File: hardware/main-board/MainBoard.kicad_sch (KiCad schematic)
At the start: 0 parts

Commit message: feat: top level schem
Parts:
- added CH446Q3: ~, symbol SeniorDesign:CH446Q_Crossbar_Switch
- added R1, R10, R11, R12, R13, R14, R15, R16, R17, R2, R20, R21, R22, R23, R3, R4, R5, R6, R7, R8, R9: R_US, symbol Device:R_US
- added SW1, SW10, SW11, SW12, SW13, SW17, SW18, SW19, SW2, SW3, SW4, SW5, SW6, SW7, SW8, SW9: SW_SPST, symbol Switch:SW_SPST
- added U0, U1, U2, U3, U4: TL071, symbol Amplifier_Operational:TL071
- added U5: STM32F091RCTx, Package_QFP:LQFP-64_10x10mm_P0.5mm, symbol MCU_ST_STM32F0:STM32F091RCTx
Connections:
- net STD/Input: now also CH446Q3.33 (Y0)
- net STD1/Input: now also CH446Q3.35 (Y1)
- new net: R13.2, U0.2 (-)
- new net: R21.2, R22.1, R23.1, U0.3 (+)
- new net: R12.1, SW10.2 (B)
- new net: R3.2, SW3.2 (B)
- new net: R1.2, R2.1, R3.1, U1.3 (+)
- new net: R2.2, SW2.2 (B)
- new net: R21.1, SW17.2 (B)
- new net: R4.2, U1.2 (-)
- new net: R5.1, SW4.2 (B)
- new net: R12.2, R14.1, R15.1, R17.1, U4.3 (+)
- new net: R10.1, R11.1, R9.2, U3.3 (+)
- new net: R11.2, SW9.2 (B)
- new net: R9.1, SW7.2 (B)
- new net: R16.2, U3.2 (-)
- new net: R14.2, SW11.2 (B)
- new net: R20.2, U4.2 (-)
- new net: R22.2, SW18.2 (B)
- new net: R10.2, SW8.2 (B)
- new net: R17.2, SW13.2 (B)
- new net: R15.2, SW12.2 (B)
- new net: R1.1, SW1.2 (B)
- new net: R8.2, U2.2 (-)
- new net: R5.2, R6.1, R7.1, U2.3 (+)
- new net: R6.2, SW5.2 (B)
- new net: U5.18 (VSS), U5.31 (VSS), U5.47 (VSS), U5.63 (VSS)
- new net: R7.2, SW6.2 (B)
- new net: R23.2, SW19.2 (B)
- new net +5V: U0.7 (V+), U1.7 (V+), U2.7 (V+), U3.7 (V+), U4.7 (V+)
- new net -5V: U0.4 (V-), U1.4 (V-), U2.4 (V-), U3.4 (V-), U4.4 (V-)
- new net GND: R13.1, R16.1, R20.1, R4.1, R8.1
- new net STD2/Input: CH446Q3.17 (Y4)
- new net STD3/Input: CH446Q3.39 (Y3)
- new net cell_0_out: SW1.1 (A), SW10.1 (A), SW17.1 (A), SW4.1 (A)
- new net cell_1_out: SW11.1 (A), SW18.1 (A), SW2.1 (A), SW7.1 (A)
- new net cell_2_out: SW12.1 (A), SW19.1 (A), SW5.1 (A), SW8.1 (A)
- new net cell_3_out: SW13.1 (A), SW3.1 (A), SW6.1 (A), SW9.1 (A)
- new net in_0: CH446Q3.31 (X0)
- new net in_1: CH446Q3.30 (X1)
- new net in_2: CH446Q3.29 (X2)
- new net in_3: CH446Q3.28 (X3)
- new net out: CH446Q3.37 (Y2)
- new net sum_012: CH446Q3.26 (X5), U0.6
- new net sum_013: CH446Q3.4 (X7), U1.6
- new net sum_023: CH446Q3.6 (X9), U2.6
- new net sum_123: CH446Q3.8 (X11), U3.6
- new net sum_1234: CH446Q3.24 (X13), U4.6
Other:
- added sheet STD2 (standard_cell.kicad_sch)
- added sheet STD3 (standard_cell.kicad_sch)
- note added: "Summing Amps"

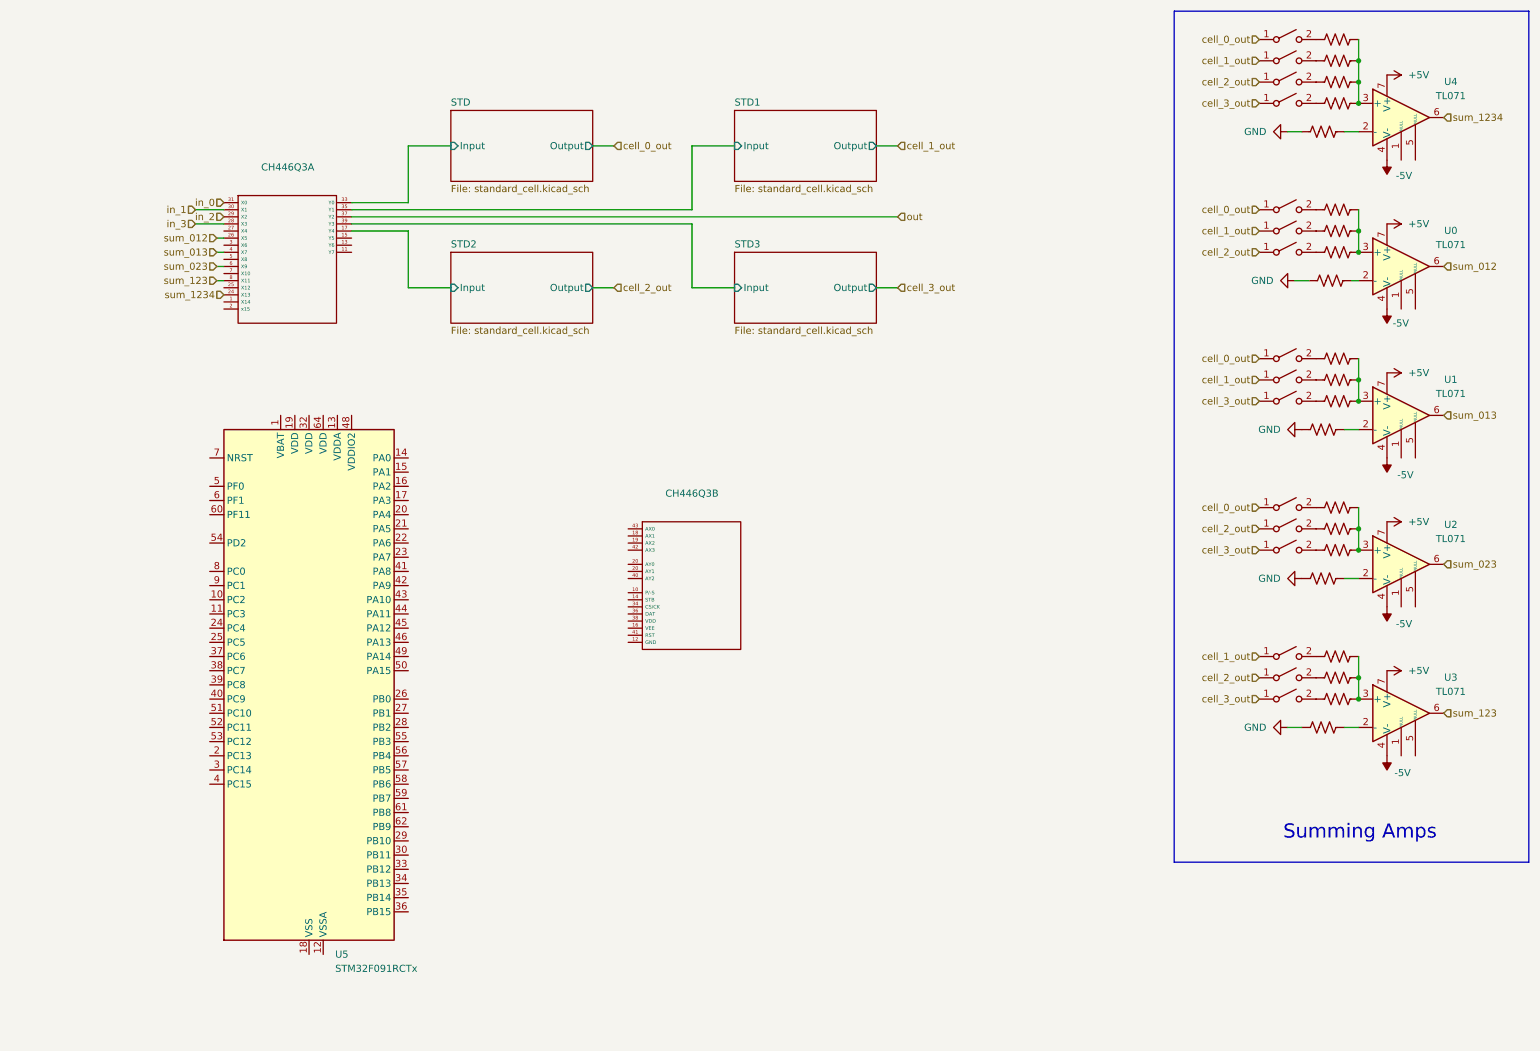
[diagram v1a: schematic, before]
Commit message: fix: top level sectioning
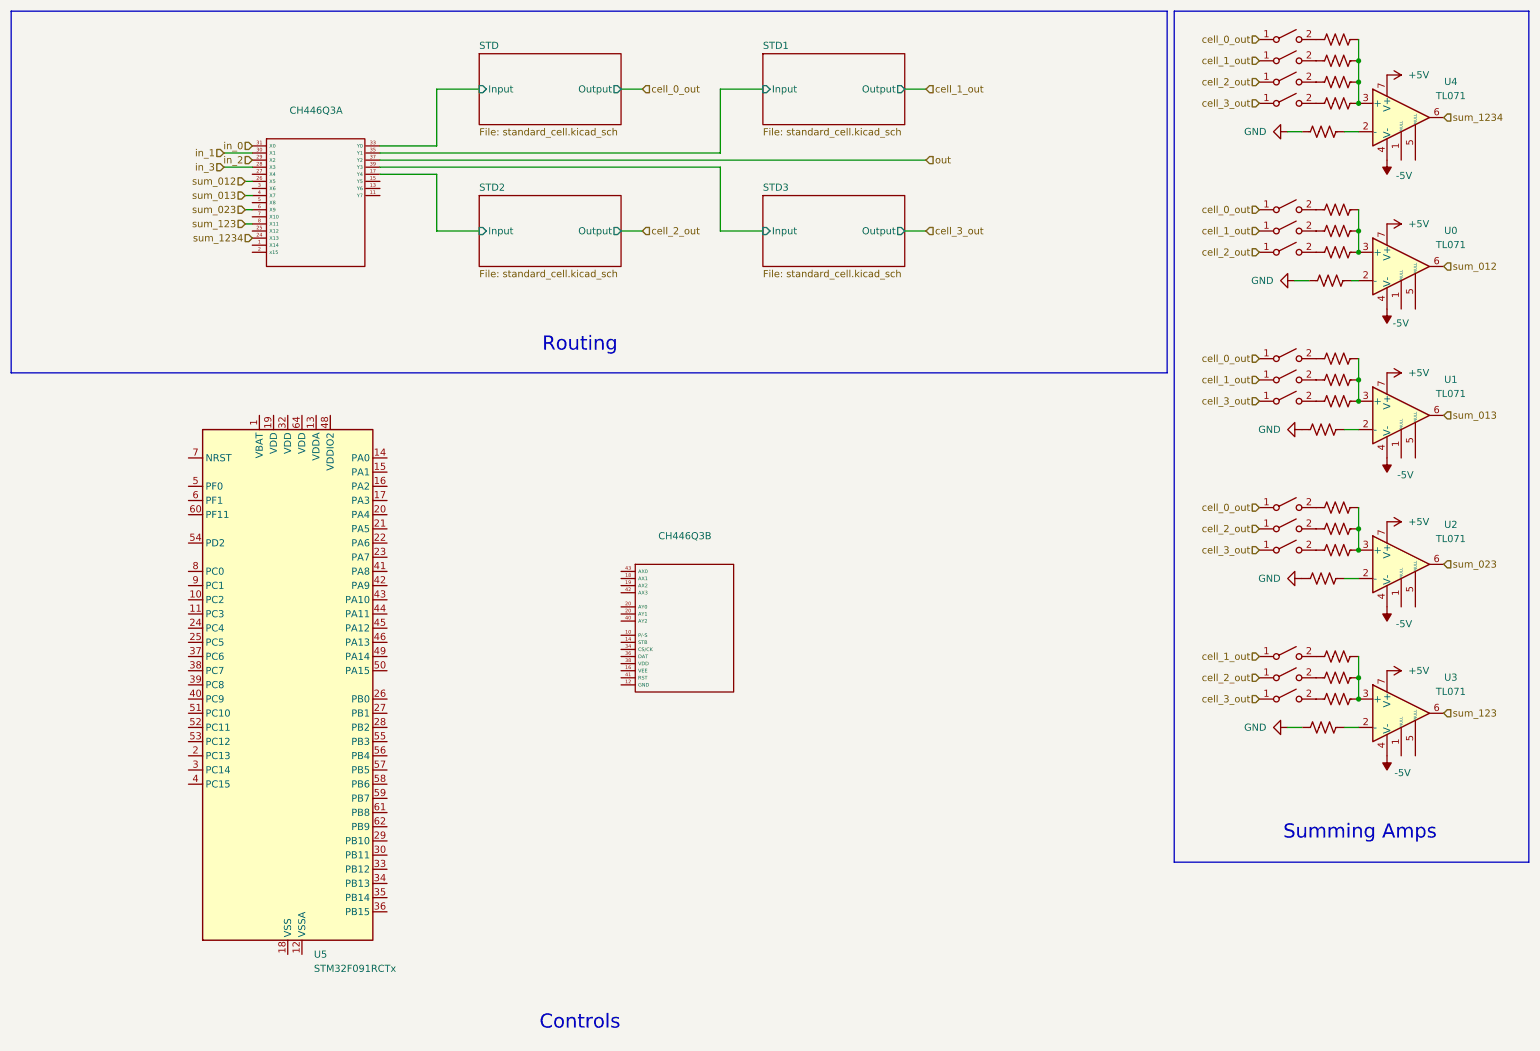
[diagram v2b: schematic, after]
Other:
- note added: "Controls"
- note added: "Routing"
- moved on the sheet: CH446Q3A, CH446Q3B, U5

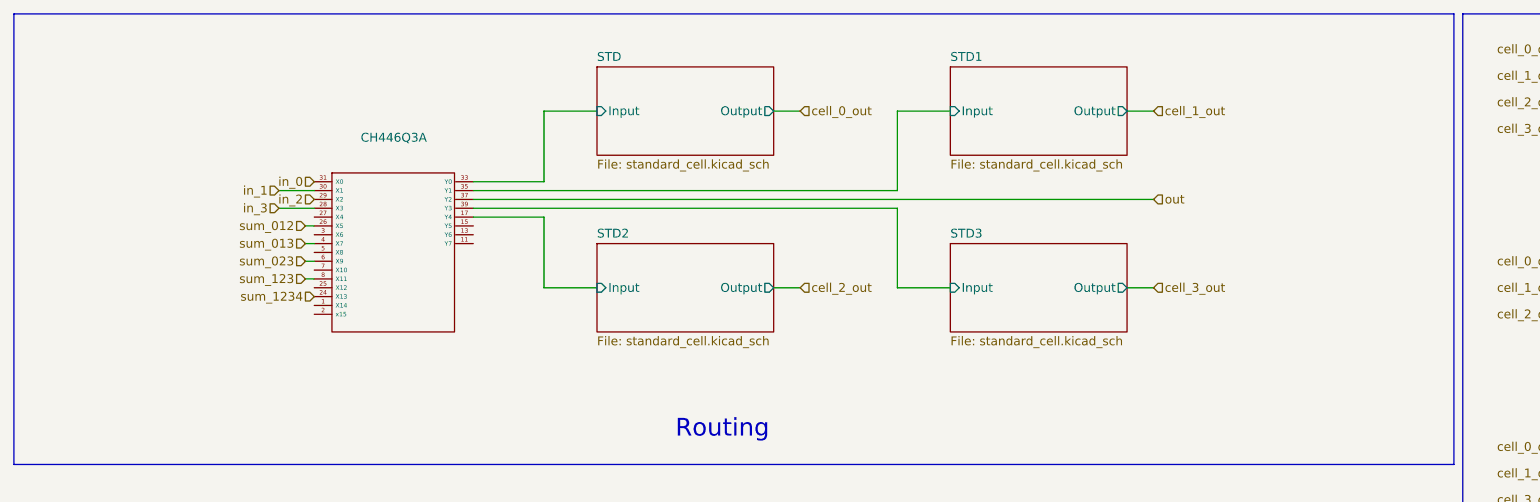
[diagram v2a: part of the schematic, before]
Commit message: feat: added power amp to top
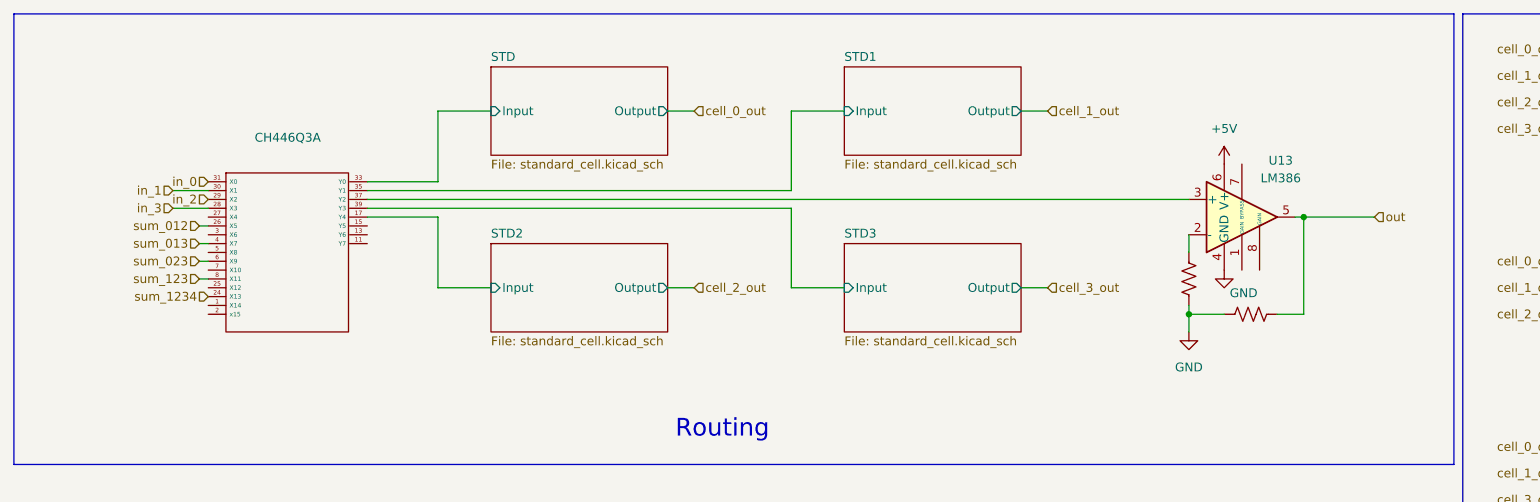
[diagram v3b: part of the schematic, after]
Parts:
- added R18, R19: R_US, symbol Device:R_US
- added U13: LM386, symbol Amplifier_Audio:LM386
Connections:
- net +5V: now also U13.6 (V+)
- net GND: now also R18.2, R19.1, U13.4 (GND)
- net out: now also R19.2, U13.5; no longer CH446Q3.37 (Y2)
- new net: R18.1, U13.2 (-)
- new net: CH446Q3.37 (Y2), U13.3 (+)
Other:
- moved on the sheet: CH446Q3A

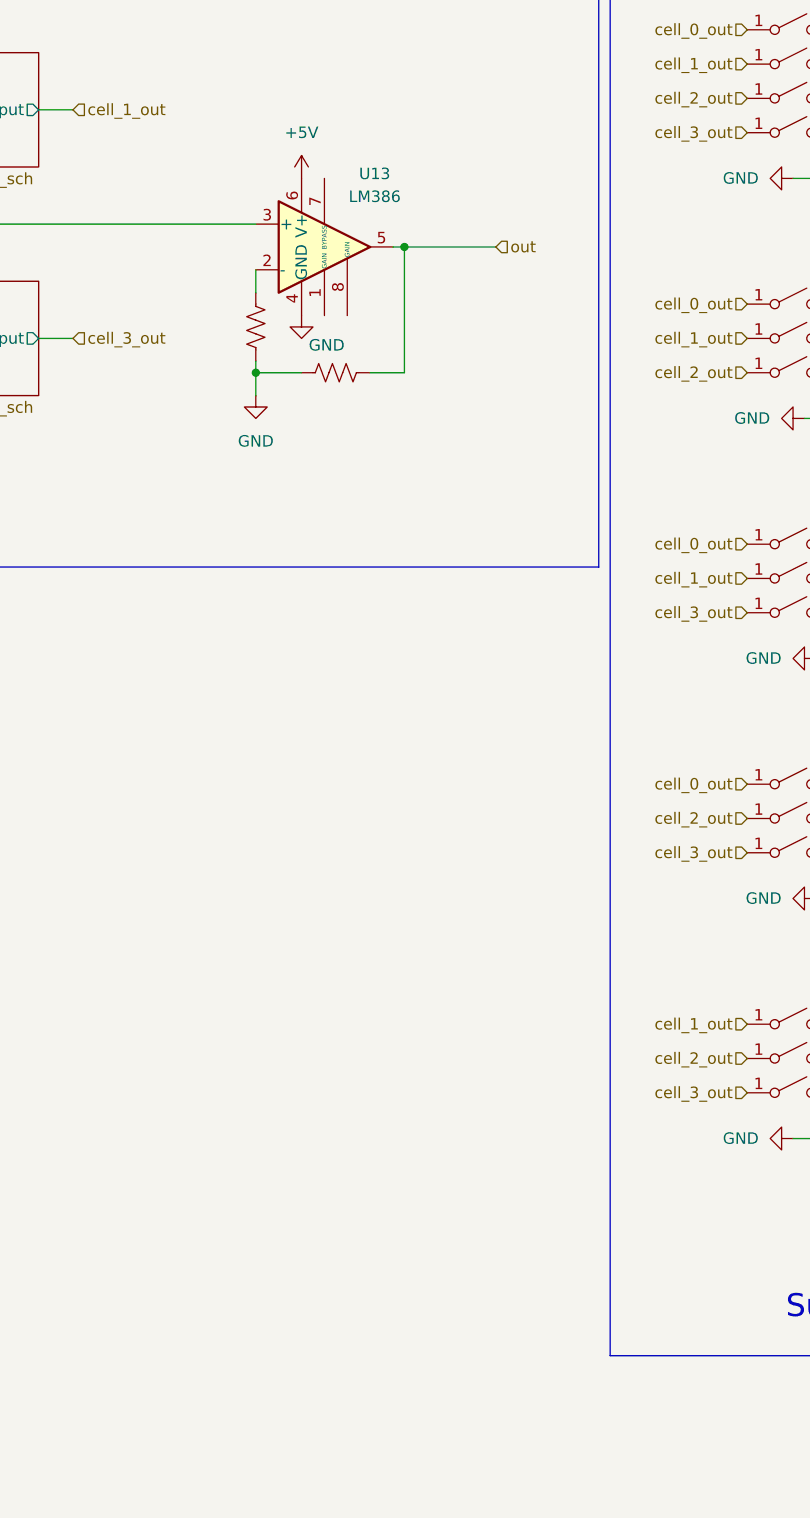
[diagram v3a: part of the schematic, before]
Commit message: Power Supply schematic added and power amp design changed. Initial Design stage.
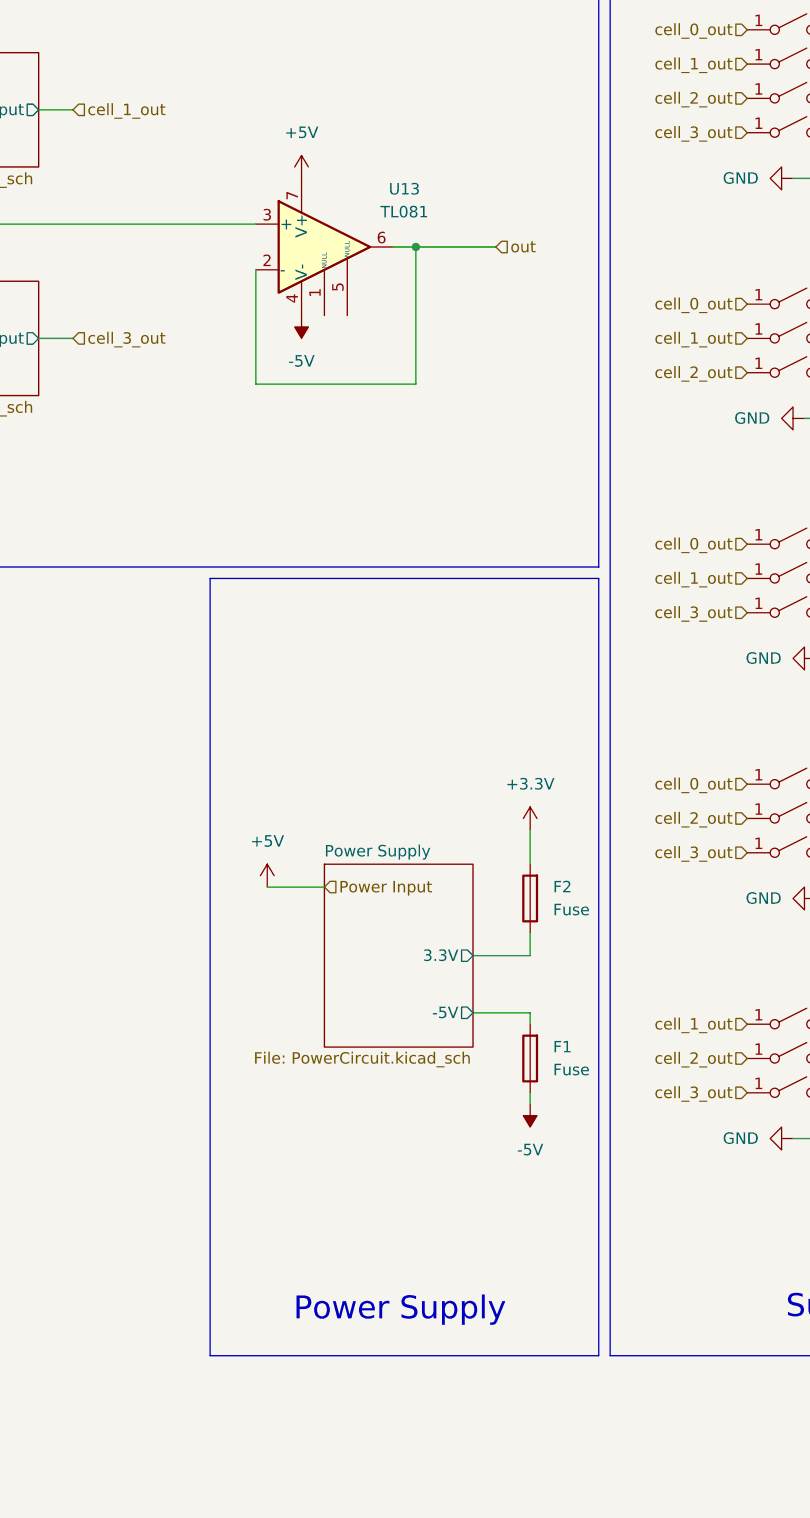
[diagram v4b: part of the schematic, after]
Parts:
- removed R18, R19: R_US, symbol Device:R_US
- removed U13: LM386, symbol Amplifier_Audio:LM386
- added F1, F2: Fuse, symbol Device:Fuse
- added U13: TL081, symbol Amplifier_Operational:TL081
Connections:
- net +5V: now also U13.7 (V+)
- net -5V: now also F1.1, U13.4 (V-)
- net out: now also U13.2 (-), U13.6
- net at CH446Q3.37 (Y2): now also U13.3 (+)
- new net +3.3V: F2.2
- new net Power Supply/-5V: F1.2
- new net Power Supply/3.3V: F2.1
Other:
- added sheet Power Supply (PowerCircuit.kicad_sch)
- note added: "Power Supply"

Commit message: Clayton's fun routing fix
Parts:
- removed R1, R10, R11, R12, R13, R14, R15, R16, R17, R2, R20, R21, R22, R23, R3, R4, R5, R6, R7, R8, R9: R_US, symbol Device:R_US
- removed SW1, SW10, SW11, SW12, SW13, SW17, SW18, SW19, SW2, SW3, SW4, SW5, SW6, SW7, SW8, SW9: SW_SPST, symbol Switch:SW_SPST
- removed U4: TL071, symbol Amplifier_Operational:TL071
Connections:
- net STD1/Input is gone; now on net Cell_0_Buff: CH446Q3.35 (Y1)
- net STD2/Input is gone; now on net Cell_3_Buff: CH446Q3.17 (Y4)
- net STD3/Input is gone; now on net Cell_2_Buff: CH446Q3.39 (Y3)
- net Cell_0_Out: now reaches U0.2 (-)
- net Cell_0_Buff: now reaches U0.3 (+)
- net Cell_0_Buff: now also U0.6
- net Cell_1_Buff: now reaches U1.3 (+)
- net Cell_1_Buff: now also CH446Q3.37 (Y2), U1.6
- net Cell_1_Out: now reaches U1.2 (-)
- net Cell_3_Buff: now reaches U3.3 (+)
- net Cell_3_Buff: now also U3.6
- net Cell_3_Out: now reaches U3.2 (-)
- net Cell_2_Out: now reaches U2.2 (-)
- net Cell_2_Buff: now reaches U2.3 (+)
- net Cell_2_Buff: now also U2.6
- net at U13.3 (+): now also CH446Q3.3 (X6); no longer CH446Q3.37 (Y2)
- net STD2/Input_3: now reaches CH446Q3.25 (X12)
- net STD1/Input_2: now reaches CH446Q3.27 (X4)
- net STD3/Input_2: now reaches CH446Q3.5 (X8)
- net STD2/Input_1: now reaches CH446Q3.7 (X10)
- net STD/Input renamed Signal_In
- net in_0 renamed STD/Input_1
- net in_1 renamed STD/Input_2
- net in_2 renamed STD/Input_3
- net in_3 renamed STD1/Input_1
- net out renamed Signal_Out
- net sum_012 renamed STD1/Input_3
- net STD1/Input_3: no longer U0.6
- net sum_013 renamed STD3/Input_1
- net STD3/Input_1: no longer U1.6
- net sum_023 renamed STD3/Input_3
- net STD3/Input_3: no longer U2.6
- net sum_123 renamed STD2/Input_2
- net STD2/Input_2: no longer U3.6
- net sum_1234: no longer names the net of CH446Q3.24 (X13)
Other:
- sheet STD ports: added Input_1, Input_2, Input_3; removed Input
- sheet STD1 ports: added Input_1, Input_2, Input_3; removed Input
- sheet STD2 ports: added Input_1, Input_2, Input_3; removed Input
- sheet STD3 ports: added Input_1, Input_2, Input_3; removed Input
- note added: "Output Buffers"
- note removed: "Summing Amps"
- moved on the sheet: U0, U1, U2, U3

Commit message: Big Changes in the Schematic World
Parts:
- removed unit 1 of CH446Q3
- added U1: MT8816AF1, MT8816AF1:QFP80P1200X1200X120-44N, symbol SeniorDesign:MT8816AF1
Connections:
- net Cell_0_Buff: now also U1.35 (Y1)
- net Cell_1_Buff: now also U1.37 (Y2)
- net Cell_2_Buff: now also U1.39 (Y3)
- net Cell_3_Buff: now also U1.17 (Y4)
- net STD/Input_1: now also U1.31 (X0)
- net STD/Input_2: now also U1.30 (X1)
- net STD/Input_3: now also U1.29 (X2)
- net STD1/Input_1: now also U1.28 (X3)
- net STD1/Input_2: now also U1.27 (X4)
- net STD1/Input_3: now also U1.26 (X5)
- net STD2/Input_1: now also U1.8 (X10)
- net STD2/Input_2: now also U1.9 (X11)
- net STD2/Input_3: now also U1.25 (X12)
- net STD3/Input_1: now also U1.5 (X7)
- net STD3/Input_2: now also U1.6 (X8)
- net STD3/Input_3: now also U1.7 (X9)
- net Signal_In: now also U1.32 (Y0)
- net at U13.3 (+): now also U1.4 (X6)

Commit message: God is Real, God is Real, Im not kidding this time I wouldn't joke about this
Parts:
- removed CH446Q3: ~, symbol SeniorDesign:CH446Q_Crossbar_Switch
- removed U5: STM32F091RCTx, Package_QFP:LQFP-64_10x10mm_P0.5mm, symbol MCU_ST_STM32F0:STM32F091RCTx
- added J4, J5, J6, J7: Conn_01x03_Pin, Connector_PinHeader_1.00mm:PinHeader_1x32_P1.00mm_Horizontal, symbol Connector:Conn_01x03_Pin
- added SW2, SW3: SW_SP3T, Button_Switch_SMD:SW_DIP_SPSTx02_Slide_6.7x6.64mm_W6.73mm_P2.54mm_LowProfile_JPin, symbol Switch:SW_SP3T
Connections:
- net Signal_In: now also SW2.3
- net Signal_Out: now also SW3.3
- new net: J4.1 (Pin_1), SW2.4
- new net: J4.2 (Pin_2), SW2.2
- new net: J4.3 (Pin_3), SW2.1
- new net: J7.3 (Pin_3), SW3.1
- new net: J7.2 (Pin_2), SW3.2
- new net: J7.1 (Pin_1), SW3.4
- new net GND: J5.1 (Pin_1), J5.2 (Pin_2), J5.3 (Pin_3), J6.1 (Pin_1), J6.2 (Pin_2), J6.3 (Pin_3)
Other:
- added sheet MicroController (stm_controls.kicad_sch)
- note added: "Inputs"
- note added: "Outputs"
